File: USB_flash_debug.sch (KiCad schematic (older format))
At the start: 30 parts

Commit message: Added footprint of 2x USB-A stacked. Added connections to USB HUB.
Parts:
- C?: footprint antmicro-footprints:0402-cap -> sc606-baseboard-footprints:0402-cap; symbol antmicroCapacitors0402:C_2u2_0402 -> sc606-baseboard:C_2u2_0402
- C?: footprint antmicro-footprints:0402-cap -> sc606-baseboard-footprints:0402-cap; symbol antmicroCapacitors0402:C_1u_0402 -> sc606-baseboard:C_1u_0402
- C? (x2): footprint antmicro-footprints:0402-cap -> sc606-baseboard-footprints:0402-cap; symbol antmicroCapacitors0402:C_47p_0402 -> sc606-baseboard:C_47p_0402
- FB?: footprint antmicro-footprints:0603 -> sc606-baseboard-footprints:0603; symbol antmicroFerriteBeadsandChips:BLM18EG221SN1D -> sc606-baseboard:BLM18EG221SN1D
- IC?: footprint antmicro-footprints:SOT-23-5 -> sc606-baseboard-footprints:SOT-23-5; symbol antmicroPMICVoltageRegulatorsLinear:TPS7A0518PDBVT -> sc606-baseboard:TPS7A0518PDBVT
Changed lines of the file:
@@
 5V0_DBG
 $Comp
-L antmicroCapacitors0402:C_2u2_0402 C?
+L sc606-baseboard:C_2u2_0402 C?
 U 1 1 61FA0F2B
 P 11850 1450
 F 0 "C?" H 11965 1495 60  0000 L CNN
 F 1 "C_2u2_0402" H 11850 1300 60  0001 C CNN
-F 2 "antmicro-footprints:0402-cap" H 12050 1650 60  0001 L CNN
+F 2 "sc606-baseboard-footprints:0402-cap" H 12050 1650 60  0001 L CNN
 F 3 "" H 11850 1450 50  0001 C CNN
 F 4 "TDK" H 12050 1850 60  0001 L CNN "Manufacturer"
@@
 $EndComp
 $Comp
-L antmicroCapacitors0402:C_1u_0402 C?
+L sc606-baseboard:C_1u_0402 C?
 U 1 1 61FA1789
 P 13450 1450
 F 0 "C?" H 13565 1495 60  0000 L CNN
 F 1 "C_1u_0402" H 13450 1300 60  0001 C CNN
-F 2 "antmicro-footprints:0402-cap" H 13650 1650 60  0001 L CNN
+F 2 "sc606-baseboard-footprints:0402-cap" H 13650 1650 60  0001 L CNN
 F 3 "" H 13450 1450 50  0001 C CNN
 F 4 "TDK" H 13650 1850 60  0001 L CNN "Manufacturer"
@@
 $EndComp
 $Comp
-L antmicroPMICVoltageRegulatorsLinear:TPS7A0518PDBVT IC?
+L sc606-baseboard:TPS7A0518PDBVT IC?
 U 1 1 61FA2014
 P 12700 1350
 F 0 "IC?" H 12700 1831 50  0000 C CNN
 F 1 "TPS7A0518PDBVT" H 12700 1748 39  0000 C CNN
-F 2 "antmicro-footprints:SOT-23-5" H 12700 1100 50  0001 C CNN
+F 2 "sc606-baseboard-footprints:SOT-23-5" H 12700 1100 50  0001 C CNN
 F 3 "" H 12700 1350 50  0001 C CNN
 F 4 "TPS7A0518PDBVT" H 12700 1665 50  0000 C CNN "MPN"
@@
 	13100 1300 13450 1300
 $Comp
-L power:GND #PWR?
+L sc606-baseboard:GND #PWR?
 U 1 1 61FD04EC
 P 13450 1600
@@
 Connection ~ 13450 1600
 $Comp
-L power:GND #PWR?
+L sc606-baseboard:GND #PWR?
 U 1 1 61FD0C36
 P 11850 1600
@@
 	12150 3150 12950 3150
 $Comp
-L antmicroCapacitors0402:C_47p_0402 C?
+L sc606-baseboard:C_47p_0402 C?
 U 1 1 61FF8CD9
 P 12200 4750
 F 0 "C?" H 12250 4850 60  0000 L CNN
 F 1 "C_47p_0402" H 12200 4600 60  0001 C CNN
-F 2 "antmicro-footprints:0402-cap" H 12400 4950 60  0001 L CNN
+F 2 "sc606-baseboard-footprints:0402-cap" H 12400 4950 60  0001 L CNN
 F 3 "" H 12200 4750 50  0001 C CNN
 F 4 "KEMET" H 12400 5150 60  0001 L CNN "Manufacturer"
@@
 $EndComp
 $Comp
-L antmicroCapacitors0402:C_47p_0402 C?
+L sc606-baseboard:C_47p_0402 C?
 U 1 1 61FF90E8
 P 11950 4750
 F 0 "C?" H 12000 4850 60  0000 L CNN
 F 1 "C_47p_0402" H 11950 4600 60  0001 C CNN
-F 2 "antmicro-footprints:0402-cap" H 12150 4950 60  0001 L CNN
+F 2 "sc606-baseboard-footprints:0402-cap" H 12150 4950 60  0001 L CNN
 F 3 "" H 11950 4750 50  0001 C CNN
 F 4 "KEMET" H 12150 5150 60  0001 L CNN "Manufacturer"
@@
 DBG_VBUS
 $Comp
-L antmicroFerriteBeadsandChips:BLM18EG221SN1D FB?
+L sc606-baseboard:BLM18EG221SN1D FB?
 U 1 1 622B828F
 P 10050 2150
 F 0 "FB?" H 10050 2437 60  0000 C CNN
 F 1 "BLM18EG221SN1D" H 10050 2331 60  0000 C CNN
-F 2 "antmicro-footprints:0603" H 10250 2350 60  0001 L CNN
+F 2 "sc606-baseboard-footprints:0603" H 10250 2350 60  0001 L CNN
 F 3 "" H 10250 2450 60  0001 L CNN
 F 4 "BLM18EG221SN1D" H 10250 2650 60  0001 L CNN "MPN"
@@
 Text Label 4750 3700 2    50   ~ 0
 USB_FLASH_5V0
-Text Label 1500 4150 2    50   ~ 0
-USB_HUB_P
-Text Label 1500 4550 2    50   ~ 0
-USB_HUB_N
 Text Label 1500 4950 2    50   ~ 0
 USB_FLASH_ENABLE
@@
 Wire Wire Line
 	12200 4900 12450 4900
+Text GLabel 1500 4550 0    50   Input ~ 0
+USB_HUB_P
+Text GLabel 1500 4150 0    50   Input ~ 0
+USB_HUB_N
 $EndSCHEMATC

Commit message: Started placing main components on PCB. Change of RT battery model and USB flash connector
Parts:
- removed J?: 1051330001, sc606-baseboard-footprints:USB_Micro_B_Female_Vert_1051330001, symbol sc606-baseboard:1051330001
- added J9: 0473460001, sc606-baseboard-footprints:USB_Micro_B_Female_0473460001, symbol sc606-baseboard:0473460001
- gave numbers to parts that had none: 29
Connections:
- net GND: now also J9.5, J9.SH
- net USB_FLASH_5V0: now also J9.1
- net USB_FLASH_N: now also J9.3
- net USB_FLASH_P: now also J9.2
- net at TP12.1: now also J9.4

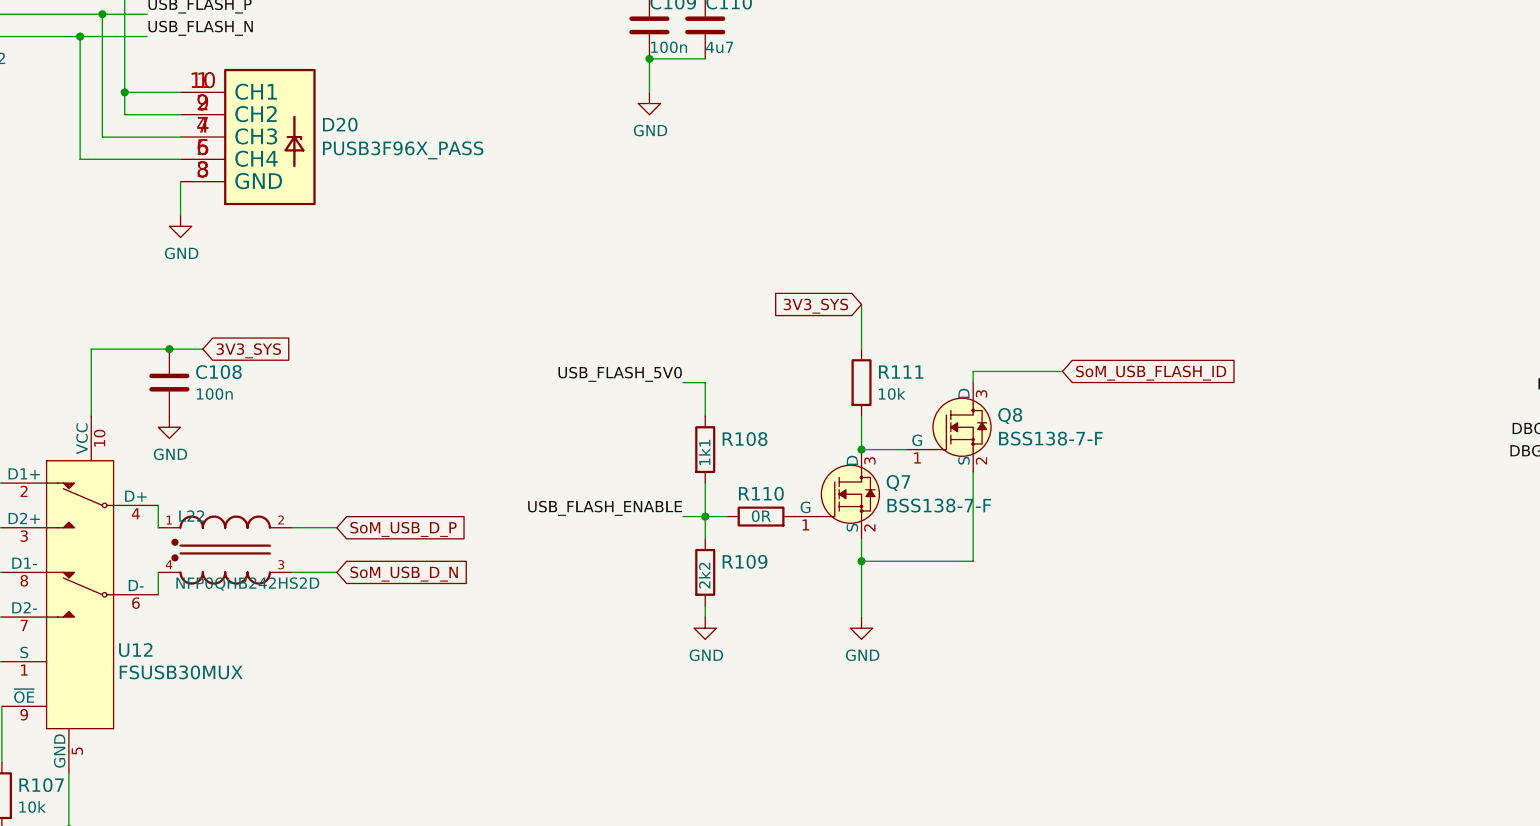
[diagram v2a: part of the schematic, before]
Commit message: FFC and general display camera connectors distributed on board
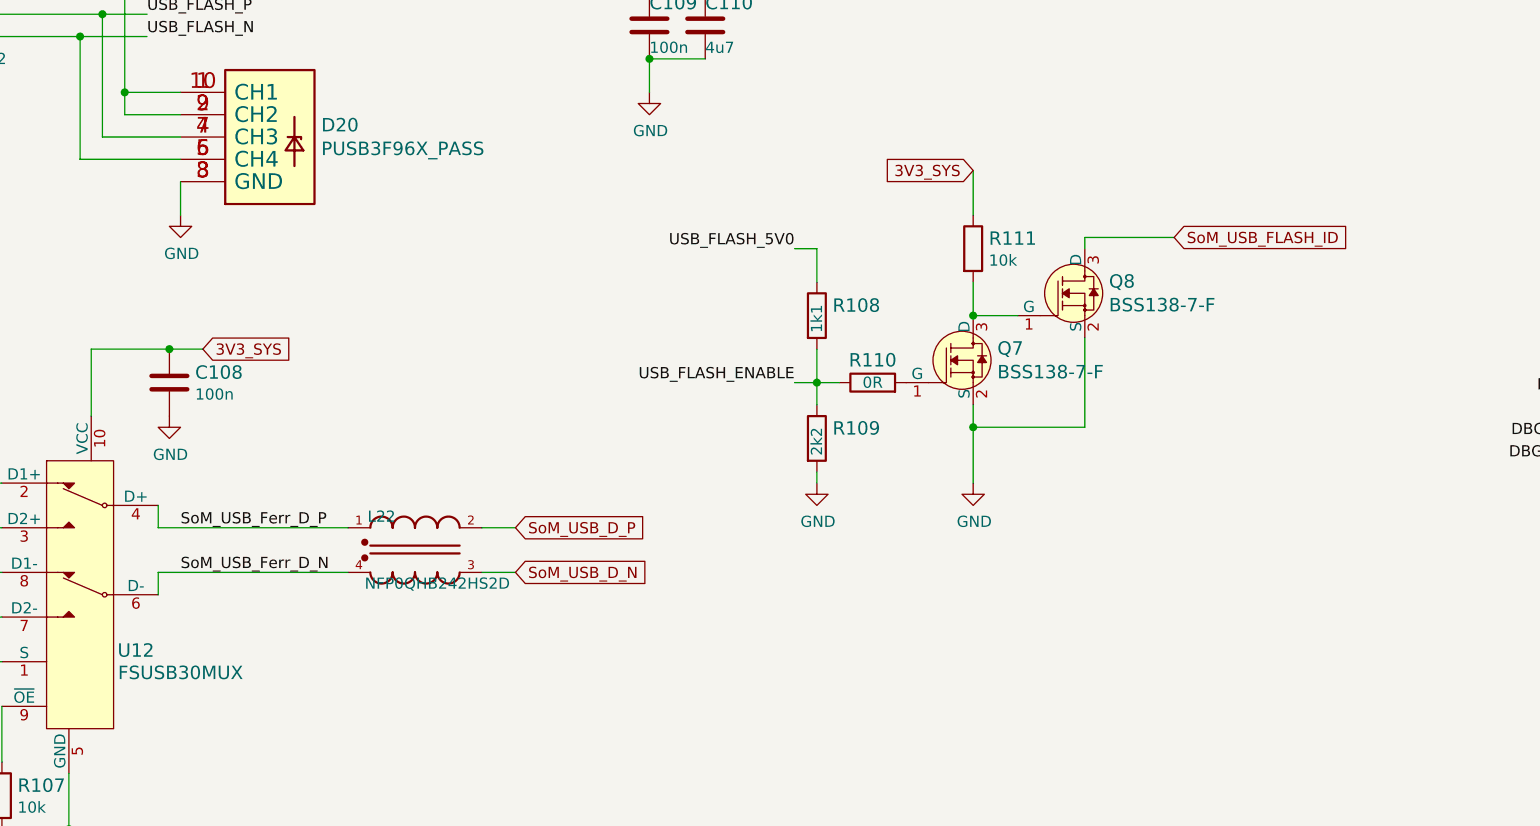
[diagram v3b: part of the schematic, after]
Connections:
- net SoM_USB_Ferr_D_P: now reaches L22.1, U12.4 (D+)
- net SoM_USB_Ferr_D_N: now reaches L22.4, U12.6 (D-)
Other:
- moved on the sheet: L22, Q7, Q8, R108, R109, R110, R111
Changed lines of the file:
@@
 	1    0    0    -1
 $EndComp
-Text GLabel 3200 4350 2    50   Input ~ 0
+Text GLabel 4000 4350 2    50   Input ~ 0
 SoM_USB_D_P
-Text GLabel 3200 4550 2    50   Input ~ 0
+Text GLabel 4000 4550 2    50   Input ~ 0
 SoM_USB_D_N
 $Comp
 L sc606-baseboard:NFP0QHB242HS2D L?
 U 1 1 62997242
-P 2700 4450
+P 3550 4450
 AR Path="/61D49FBF/62997242" Ref="L?"  Part="1"
 AR Path="/61F60810/62997242" Ref="L22"  Part="1"
-F 0 "L22" H 2550 4600 50  0000 C CNN
-F 1 "NFP0QHB242HS2D" H 2800 4300 50  0000 C CNN
-F 2 "sc606-baseboard-footprints:FIL_NFP0QHB242HS2D" H 2455 4780 50  0001 C CNN
-F 3 "https://www.farnell.com/datasheets/2616945.pdf" H 2700 4450 50  0001 C CNN
-F 4 "NFP0QHB242HS2D" H 2700 4767 50  0001 C CNN "MPN"
-F 5 "MURATA" H 2700 4676 50  0001 C CNN "Manufacturer"
-	1    2700 4450
-	1    0    0    -1
-$EndComp
-Wire Wire Line
-	3000 4350 3200 4350
-Wire Wire Line
-	3000 4550 3200 4550
-Wire Wire Line
-	2400 4350 2400 4250
-Wire Wire Line
-	2400 4550 2400 4650
+F 0 "L22" H 3400 4600 50  0000 C CNN
+F 1 "NFP0QHB242HS2D" H 3650 4300 50  0000 C CNN
+F 2 "sc606-baseboard-footprints:FIL_NFP0QHB242HS2D" H 3305 4780 50  0001 C CNN
+F 3 "https://www.farnell.com/datasheets/2616945.pdf" H 3550 4450 50  0001 C CNN
+F 4 "NFP0QHB242HS2D" H 3550 4767 50  0001 C CNN "MPN"
+F 5 "MURATA" H 3550 4676 50  0001 C CNN "Manufacturer"
+	1    3550 4450
+	1    0    0    -1
+$EndComp
+Wire Wire Line
+	3850 4350 4000 4350
+Wire Wire Line
+	3850 4550 4000 4550
 Text GLabel 2600 3550 2    50   Input ~ 0
 3V3_SYS
@@
 L sc606-baseboard:GND #PWR0122
 U 1 1 62A2E7F1
-P 4850 4750
-F 0 "#PWR0122" H 4850 4500 50  0001 C CNN
-F 1 "GND" H 4855 4577 50  0000 C CNN
-F 2 "" H 4850 4750 50  0001 C CNN
-F 3 "" H 4850 4750 50  0001 C CNN
-	1    4850 4750
+P 5350 4150
+F 0 "#PWR0122" H 5350 3900 50  0001 C CNN
+F 1 "GND" H 5355 3977 50  0000 C CNN
+F 2 "" H 5350 4150 50  0001 C CNN
+F 3 "" H 5350 4150 50  0001 C CNN
+	1    5350 4150
 	1    0    0    -1
 $EndComp
@@
 L sc606-baseboard:R_1k1_0402 R108
 U 1 1 62A2F52B
-P 4850 4000
-F 0 "R108" V 4805 4070 60  0000 L CNN
-F 1 "R_1k1_0402" H 4850 3850 60  0001 C CNN
-F 2 "sc606-baseboard-footprints:0402-res" H 5050 4200 60  0001 L CNN
-F 3 "" H 4850 4000 50  0001 C CNN
-F 4 "PANASONIC_ELECTRONIC_COMPONENTS" H 5050 4400 60  0001 L CNN "Manufacturer"
-F 5 "ERJ2RKF1101X" H 5050 4300 60  0001 L CNN "MPN"
-F 6 "1k1" H 4800 4000 50  0000 L CNN "Val"
-	1    4850 4000
+P 5350 3400
+F 0 "R108" V 5305 3470 60  0000 L CNN
+F 1 "R_1k1_0402" H 5350 3250 60  0001 C CNN
+F 2 "sc606-baseboard-footprints:0402-res" H 5550 3600 60  0001 L CNN
+F 3 "" H 5350 3400 50  0001 C CNN
+F 4 "PANASONIC_ELECTRONIC_COMPONENTS" H 5550 3800 60  0001 L CNN "Manufacturer"
+F 5 "ERJ2RKF1101X" H 5550 3700 60  0001 L CNN "MPN"
+F 6 "1k1" H 5300 3400 50  0000 L CNN "Val"
+	1    5350 3400
 	0    1    1    0
 $EndComp
@@
 L sc606-baseboard:R_2k2_0402 R109
 U 1 1 62A3038C
-P 4850 4550
-F 0 "R109" V 4805 4620 60  0000 L CNN
-F 1 "R_2k2_0402" H 4850 4400 60  0001 C CNN
-F 2 "sc606-baseboard-footprints:0402-res" H 5050 4750 60  0001 L CNN
-F 3 "" H 4850 4550 50  0001 C CNN
-F 4 "YAGEO" H 5050 4950 60  0001 L CNN "Manufacturer"
-F 5 "RC0402FR-072K2L" H 5050 4850 60  0001 L CNN "MPN"
-F 6 "2k2" H 4800 4550 50  0000 L CNN "Val"
-	1    4850 4550
+P 5350 3950
+F 0 "R109" V 5305 4020 60  0000 L CNN
+F 1 "R_2k2_0402" H 5350 3800 60  0001 C CNN
+F 2 "sc606-baseboard-footprints:0402-res" H 5550 4150 60  0001 L CNN
+F 3 "" H 5350 3950 50  0001 C CNN
+F 4 "YAGEO" H 5550 4350 60  0001 L CNN "Manufacturer"
+F 5 "RC0402FR-072K2L" H 5550 4250 60  0001 L CNN "MPN"
+F 6 "2k2" H 5300 3950 50  0000 L CNN "Val"
+	1    5350 3950
 	0    1    1    0
 $EndComp
 Wire Wire Line
-	4850 4750 4850 4700
-Wire Wire Line
-	4850 3700 4750 3700
-Wire Wire Line
-	4850 3700 4850 3850
-Wire Wire Line
-	4750 4300 4850 4300
-Connection ~ 4850 4300
-Wire Wire Line
-	4850 4300 4850 4150
-Wire Wire Line
-	4850 4300 4850 4400
-Wire Wire Line
-	4950 4300 4850 4300
-Wire Wire Line
-	5550 4750 5550 4500
+	5350 4150 5350 4100
+Wire Wire Line
+	5350 3100 5250 3100
+Wire Wire Line
+	5350 3100 5350 3250
+Wire Wire Line
+	5250 3700 5350 3700
+Connection ~ 5350 3700
+Wire Wire Line
+	5350 3700 5350 3550
+Wire Wire Line
+	5350 3700 5350 3800
+Wire Wire Line
+	5450 3700 5350 3700
+Wire Wire Line
+	6050 4150 6050 3900
 $Comp
 L sc606-baseboard:GND #PWR0123
 U 1 1 62A39278
-P 5550 4750
-F 0 "#PWR0123" H 5550 4500 50  0001 C CNN
-F 1 "GND" H 5555 4577 50  0000 C CNN
-F 2 "" H 5550 4750 50  0001 C CNN
-F 3 "" H 5550 4750 50  0001 C CNN
-	1    5550 4750
-	1    0    0    -1
-$EndComp
-Text GLabel 6450 3650 2    50   Input ~ 0
+P 6050 4150
+F 0 "#PWR0123" H 6050 3900 50  0001 C CNN
+F 1 "GND" H 6055 3977 50  0000 C CNN
+F 2 "" H 6050 4150 50  0001 C CNN
+F 3 "" H 6050 4150 50  0001 C CNN
+	1    6050 4150
+	1    0    0    -1
+$EndComp
+Text GLabel 6950 3050 2    50   Input ~ 0
 SoM_USB_FLASH_ID
 $Comp
 L sc606-baseboard:R_0R_0402 R110
 U 1 1 62A4008D
-P 5100 4300
-F 0 "R110" H 5100 4400 60  0000 C CNN
-F 1 "R_0R_0402" H 5100 4150 60  0001 C CNN
-F 2 "sc606-baseboard-footprints:0402-res" H 5300 4500 60  0001 L CNN
-F 3 "" H 5100 4300 50  0001 C CNN
-F 4 "PANASONIC" H 5300 4700 60  0001 L CNN "Manufacturer"
-F 5 "ERJ2GE0R00X" H 5300 4600 60  0001 L CNN "MPN"
-F 6 "0R" H 5100 4300 50  0000 C CNN "Val"
-	1    5100 4300
+P 5600 3700
+F 0 "R110" H 5600 3800 60  0000 C CNN
+F 1 "R_0R_0402" H 5600 3550 60  0001 C CNN
+F 2 "sc606-baseboard-footprints:0402-res" H 5800 3900 60  0001 L CNN
+F 3 "" H 5600 3700 50  0001 C CNN
+F 4 "PANASONIC" H 5800 4100 60  0001 L CNN "Manufacturer"
+F 5 "ERJ2GE0R00X" H 5800 4000 60  0001 L CNN "MPN"
+F 6 "0R" H 5600 3700 50  0000 C CNN "Val"
+	1    5600 3700
 	1    0    0    -1
 $EndComp
@@
 L sc606-baseboard:BSS138-7-F Q7
 U 1 1 62A49D1F
-P 5550 4200
-F 0 "Q7" H 5658 4253 60  0000 L CNN
-F 1 "BSS138-7-F" H 5658 4147 60  0000 L CNN
-F 2 "sc606-baseboard-footprints:SOT-23-3" H 5750 4400 60  0001 L CNN
-F 3 "https://www.diodes.com/assets/Datasheets/ds30144.pdf" H 5750 4500 60  0001 L CNN
-F 4 "BSS138-7-F" H 5750 4700 60  0001 L CNN "MPN"
-F 5 "Diodes Incorporated" H 5750 5300 60  0001 L CNN "Manufacturer"
-	1    5550 4200
+P 6050 3600
+F 0 "Q7" H 6158 3653 60  0000 L CNN
+F 1 "BSS138-7-F" H 6158 3547 60  0000 L CNN
+F 2 "sc606-baseboard-footprints:SOT-23-3" H 6250 3800 60  0001 L CNN
+F 3 "https://www.diodes.com/assets/Datasheets/ds30144.pdf" H 6250 3900 60  0001 L CNN
+F 4 "BSS138-7-F" H 6250 4100 60  0001 L CNN "MPN"
+F 5 "Diodes Incorporated" H 6250 4700 60  0001 L CNN "Manufacturer"
+	1    6050 3600
 	1    0    0    -1
 $EndComp
@@
 L sc606-baseboard:BSS138-7-F Q8
 U 1 1 62A4B7F6
-P 6050 3900
-F 0 "Q8" H 6158 3953 60  0000 L CNN
-F 1 "BSS138-7-F" H 6158 3847 60  0000 L CNN
-F 2 "sc606-baseboard-footprints:SOT-23-3" H 6250 4100 60  0001 L CNN
-F 3 "https://www.diodes.com/assets/Datasheets/ds30144.pdf" H 6250 4200 60  0001 L CNN
-F 4 "BSS138-7-F" H 6250 4400 60  0001 L CNN "MPN"
-F 5 "Diodes Incorporated" H 6250 5000 60  0001 L CNN "Manufacturer"
-	1    6050 3900
-	1    0    0    -1
-$EndComp
-Wire Wire Line
-	5750 4000 5550 4000
-Wire Wire Line
-	6050 4100 6050 4500
-Wire Wire Line
-	6050 4500 5550 4500
-Connection ~ 5550 4500
-Wire Wire Line
-	5550 4500 5550 4400
-Wire Wire Line
-	6050 3650 6050 3700
-Wire Wire Line
-	6050 3650 6450 3650
-Text GLabel 5550 3350 0    50   Input ~ 0
+P 6550 3300
+F 0 "Q8" H 6658 3353 60  0000 L CNN
+F 1 "BSS138-7-F" H 6658 3247 60  0000 L CNN
+F 2 "sc606-baseboard-footprints:SOT-23-3" H 6750 3500 60  0001 L CNN
+F 3 "https://www.diodes.com/assets/Datasheets/ds30144.pdf" H 6750 3600 60  0001 L CNN
+F 4 "BSS138-7-F" H 6750 3800 60  0001 L CNN "MPN"
+F 5 "Diodes Incorporated" H 6750 4400 60  0001 L CNN "Manufacturer"
+	1    6550 3300
+	1    0    0    -1
+$EndComp
+Wire Wire Line
+	6250 3400 6050 3400
+Wire Wire Line
+	6550 3500 6550 3900
+Wire Wire Line
+	6550 3900 6050 3900
+Connection ~ 6050 3900
+Wire Wire Line
+	6050 3900 6050 3800
+Wire Wire Line
+	6550 3050 6550 3100
+Wire Wire Line
+	6550 3050 6950 3050
+Text GLabel 6050 2750 0    50   Input ~ 0
 3V3_SYS
 $Comp
 L sc606-baseboard:R_10k_0402 R111
 U 1 1 62A4EC7F
-P 5550 3700
-F 0 "R111" V 5505 3770 60  0000 L CNN
-F 1 "R_10k_0402" H 5550 3550 60  0001 C CNN
-F 2 "sc606-baseboard-footprints:0402-res" H 5750 3900 60  0001 L CNN
-F 3 "" H 5550 3700 50  0001 C CNN
-F 4 "VISHAY" H 5750 4100 60  0001 L CNN "Manufacturer"
-F 5 "CRCW040210K0FKEDHP" H 5750 4000 60  0001 L CNN "MPN"
-F 6 "10k" V 5603 3770 50  0000 L CNN "Val"
-	1    5550 3700
+P 6050 3100
+F 0 "R111" V 6005 3170 60  0000 L CNN
+F 1 "R_10k_0402" H 6050 2950 60  0001 C CNN
+F 2 "sc606-baseboard-footprints:0402-res" H 6250 3300 60  0001 L CNN
+F 3 "" H 6050 3100 50  0001 C CNN
+F 4 "VISHAY" H 6250 3500 60  0001 L CNN "Manufacturer"
+F 5 "CRCW040210K0FKEDHP" H 6250 3400 60  0001 L CNN "MPN"
+F 6 "10k" V 6103 3170 50  0000 L CNN "Val"
+	1    6050 3100
 	0    1    1    0
 $EndComp
 Wire Wire Line
-	5550 3550 5550 3350
-Wire Wire Line
-	5550 3850 5550 4000
-Connection ~ 5550 4000
+	6050 2950 6050 2750
+Wire Wire Line
+	6050 3250 6050 3400
+Connection ~ 6050 3400
 $Comp
 L sc606-baseboard:1X03 SW1
@@
 Text Label 4400 1950 2    50   ~ 0
 USB_FLASH_5V0
-Text Label 4750 3700 2    50   ~ 0
+Text Label 5250 3100 2    50   ~ 0
 USB_FLASH_5V0
 Text Label 1500 4950 2    50   ~ 0
 USB_FLASH_ENABLE
-Text Label 4750 4300 2    50   ~ 0
+Text Label 5250 3700 2    50   ~ 0
 USB_FLASH_ENABLE
 Text Label 10400 1450 0    50   ~ 0
@@
 	1    0    0    -1
 $EndComp
+Wire Wire Line
+	3250 4350 2400 4350
+Wire Wire Line
+	2400 4350 2400 4250
+Wire Wire Line
+	3250 4550 2400 4550
+Wire Wire Line
+	2400 4550 2400 4650
+Text Label 2500 4350 0    50   ~ 0
+SoM_USB_Ferr_D_P
+Text Label 2500 4550 0    50   ~ 0
+SoM_USB_Ferr_D_N
 $EndSCHEMATC

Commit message: Prepared layout of USB flash and debug components
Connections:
- net DBG_USB_D_N: now also D21.1 (CH1); no longer D21.2 (CH2)
- net DBG_USB_D_P: now also D21.2 (CH2); no longer D21.1 (CH1)
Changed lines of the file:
@@
 	1    0    0    -1
 $EndComp
+Text Label 9700 5550 2    50   ~ 0
+DBG_USB_D_P
 Text Label 9700 5450 2    50   ~ 0
-DBG_USB_D_P
-Text Label 9700 5550 2    50   ~ 0
 DBG_USB_D_N
 Wire Wire Line

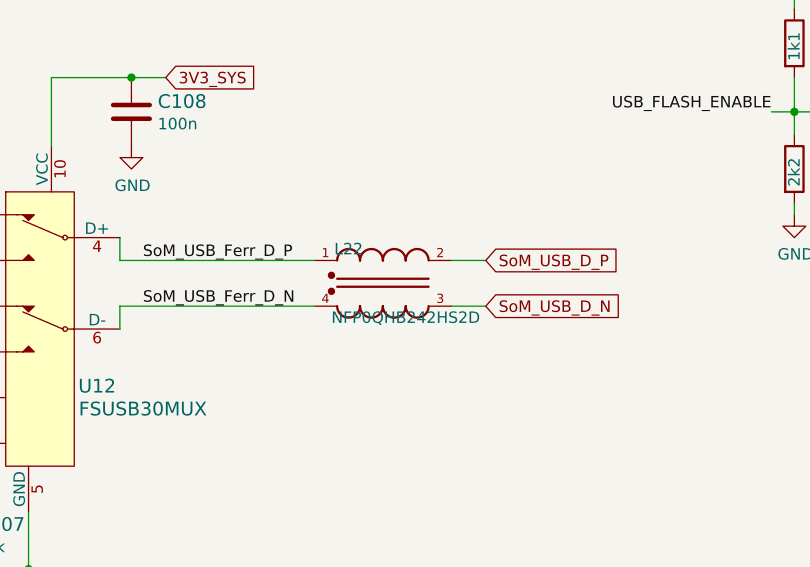
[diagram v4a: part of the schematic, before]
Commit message: All components placed on board
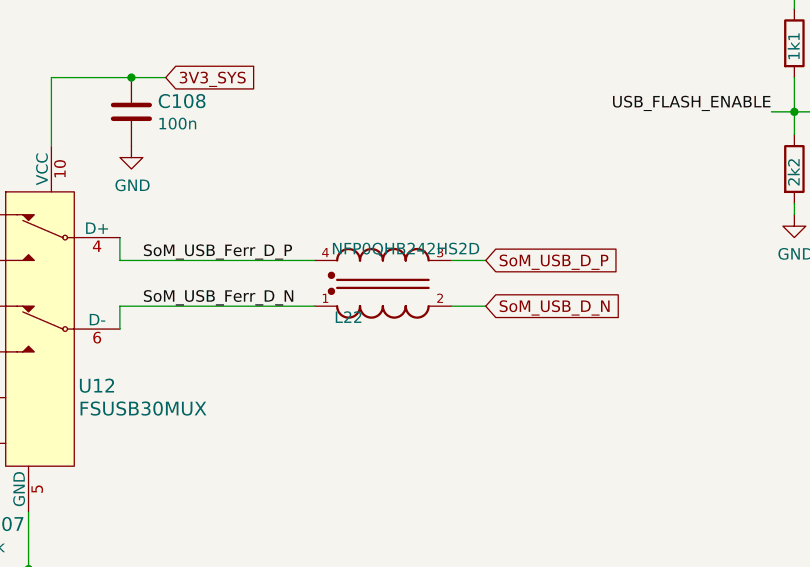
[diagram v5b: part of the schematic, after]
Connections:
- net SoM_USB_D_N: now also L22.2; no longer L22.3
- net SoM_USB_D_P: now also L22.3; no longer L22.2
- net SoM_USB_Ferr_D_N: now also L22.1; no longer L22.4
- net SoM_USB_Ferr_D_P: now also L22.4; no longer L22.1
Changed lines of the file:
@@
 F 5 "MURATA" H 3550 4676 50  0001 C CNN "Manufacturer"
 	1    3550 4450
-	1    0    0    -1
+	1    0    0    1
 $EndComp
 Wire Wire Line
